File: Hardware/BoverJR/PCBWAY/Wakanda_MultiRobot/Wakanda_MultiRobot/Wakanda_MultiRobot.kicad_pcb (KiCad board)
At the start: 2 copper layers, 50 x 50 mm, 33 parts, among them J1 Alimentacion, J10 I2C, J11 M1, J12 M2, J14 RANDOM, J2 Conn_01X03, J3 Sensor Distancia 1, J4 Conn_01X03, J5 Conn_01X03, J6 Conn_01X03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

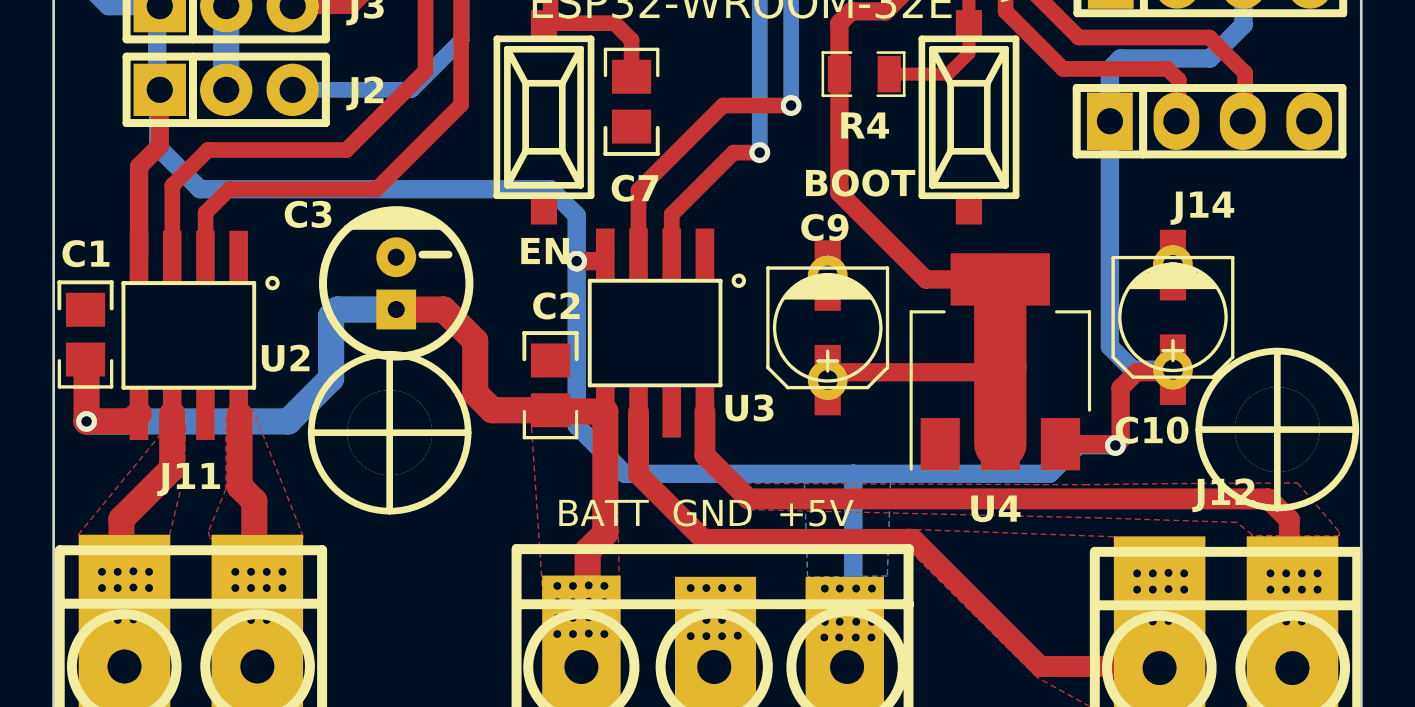
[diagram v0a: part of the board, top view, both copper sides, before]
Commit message: agregue pads a ic tb67
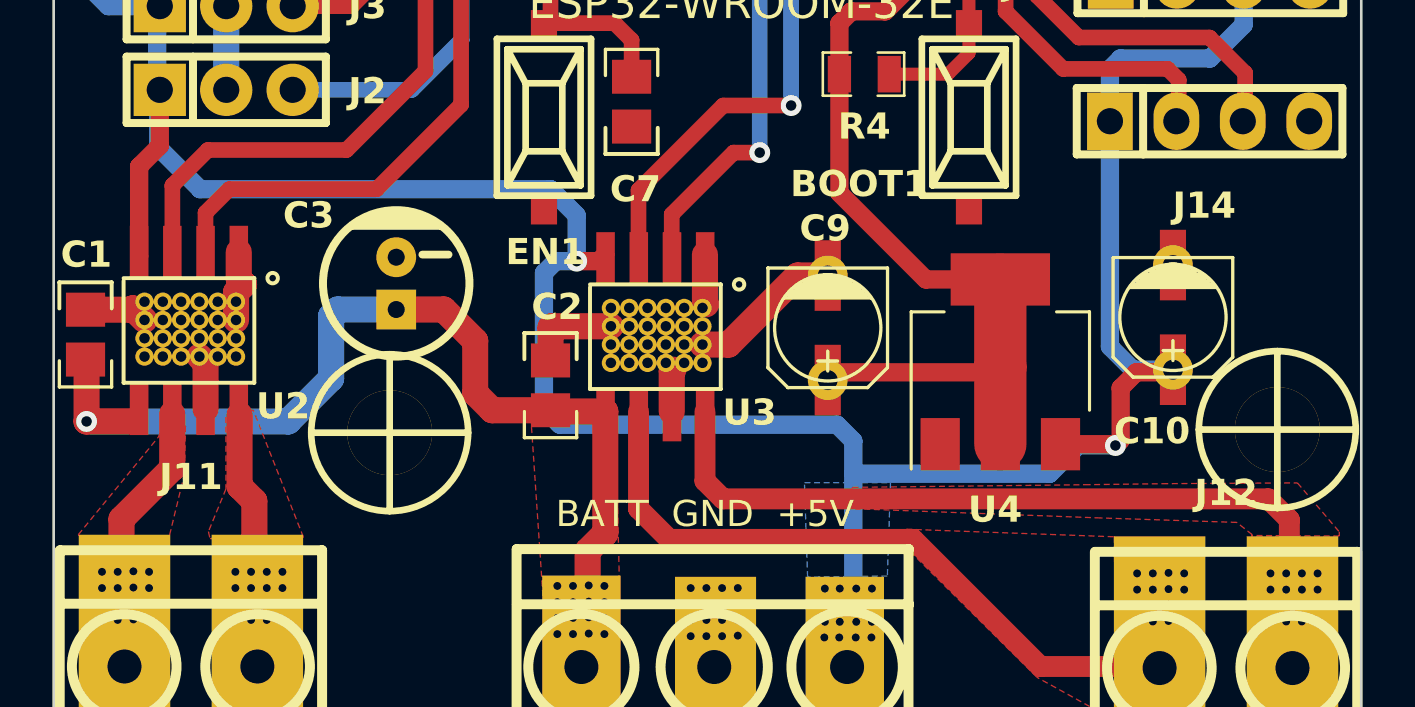
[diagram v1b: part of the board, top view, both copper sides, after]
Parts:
- U2, U3: footprint EESTN5:SSOP-8 -> EESTN5-v2:SSOP-8_disipa
- moved U2 0.19 mm to (145.2, 93.4)
- moved U3 0.14 mm to (163.0, 93.6)
- renumbered BOOT to BOOT1, EN to EN1
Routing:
- net GND: track 3.28 -> 23.7 mm
- net +5V: track 145.4 -> 148.0 mm
- net Net-(U3-OUT1): track 25.3 -> 26.0 mm
- net Net-(U3-OUT2): track 30.7 -> 31.2 mm

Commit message: cambios a wakanda en pcb
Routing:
- net /SCL: track 26.2 -> 23.9 mm
- net Vin: track 40.2 -> 38.8 mm
- net /SENSOR3: track 9.87 -> 10.9 mm
- net +5V: track 148.0 -> 147.2 mm

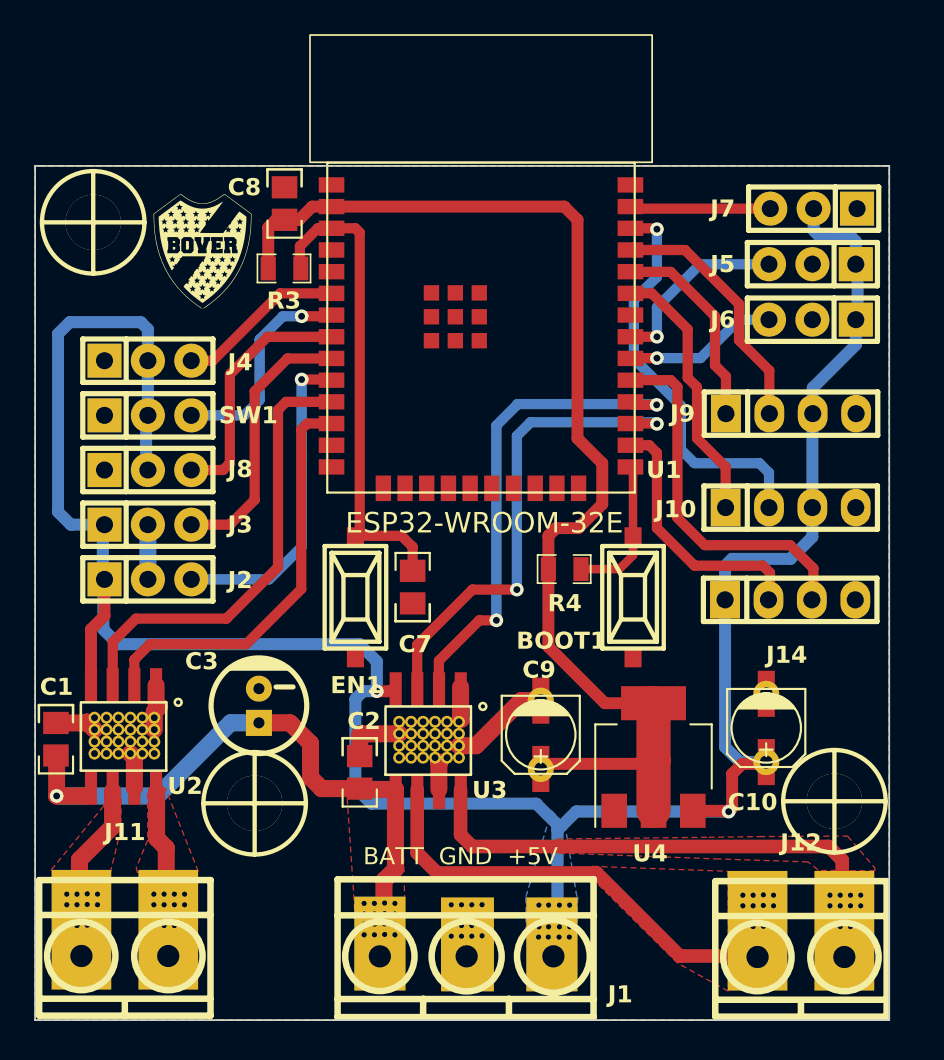
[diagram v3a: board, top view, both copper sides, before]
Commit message: esperando verificacion de pcbway ya cargue 6 gerber
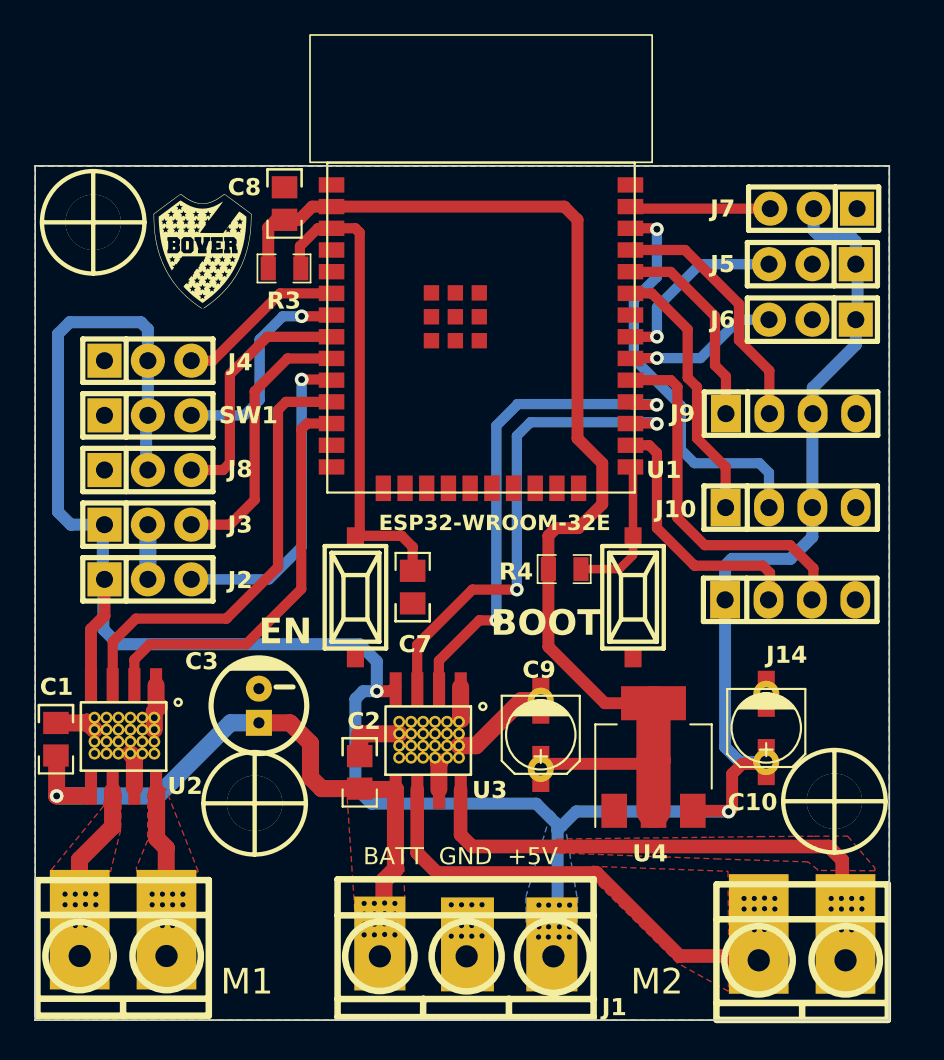
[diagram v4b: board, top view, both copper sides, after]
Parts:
- J11: footprint EESTN5:BORNERA2_AZUL -> EESTN5:BORNERA2_AZUL_VIAS
- J12: footprint EESTN5-v2:BORNERA2_AZUL_VIAS -> EESTN5:BORNERA2_AZUL_VIAS
- moved J12 0.20 mm to (184.9, 106.5)
- moved J11 0.10 mm to (145.2, 106.2)
- renumbered BOOT1 to BOOT, EN1 to EN

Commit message: agrego cambios de gerber antes de fabricar que colgue
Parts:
- removed BOOT: SW_Push, EESTN5:Pulsador_SMD_2_BAJO
- added BOOT1: BOOT, EESTN5:Pulsador_SMD_2_BAJO, F.Cu at (175.1, 85.2)
- EN1: renamed from EN; value SW_Push -> EN
- J1: footprint EESTN5-v2:BORNERA3_AZUL_VIAS -> EESTN5:BORNERA3_AZUL_VIAS
- J7: value TATAMI Frontal Derecho -> TATAMI Frontal Izquierdo
- J8: value TATAMI Frontal Izquierdo -> ~
- moved SW1 4.50 mm to (146.6, 70.1), turned to 180 degrees
- moved J4 3.20 mm to (146.6, 74.6)
- moved J9 0.90 mm to (184.2, 73.6)
- moved J1 0.24 mm to (165.2, 106.0)
- moved J5 0.11 mm to (185.6, 65.8)
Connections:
- net /TATAMI_FD renamed /SENSOR6
- net /TATAMI_FI renamed /SENSOR7
- J4 pad 1: GND -> +5V
- J4 pad 2: +5V -> GND
- J5 pad 1: +5V -> GND
- J5 pad 2: GND -> +5V
- J6 pad 1: +5V -> GND
- J6 pad 2: GND -> +5V
- J8 pad 1: GND -> +5V
- J8 pad 2: +5V -> GND
- SW1 pad 2: +5V -> /START
- SW1 pad 3: /START -> +5V
- U1 pad 10: /SENSOR5 -> /START
- U1 pad 11: /START -> /SENSOR5
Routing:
- net +5V: track 147.2 -> 127.5 mm
- net GND: track 23.7 -> 35.9 mm
- net /SENSOR5: track 9.84 -> 12.7 mm, vias 0 -> 1
- net /TXD: track 14.8 -> 13.9 mm
- net /RXD: track 12.0 -> 11.1 mm
- net /START: track 12.7 -> 13.1 mm, vias 1 -> 0
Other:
- board text added: "+5V G34 GND"
- board text added: "+5V G4 G5 GND"
- board text added: "+5V GND IO"
- board text added: "BOOT"
- board text added: "EN"
- board text added: "GPIO35 GPIO32 GPIO33 GPIO25"
- board text added: "I2C"
- board text added: "IO +5V GND"
- board text added: "RX TX GND +5V"
- board text added: "SDA SCL GND +5V"
